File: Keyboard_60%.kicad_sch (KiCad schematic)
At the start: 50 parts, among them J3 Prog_conn, J5 Tag connect TC2030-CTX, SW2 Reset Switch, U3 nRF52840-QIAA-R/nRF52833-QIAA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, Y1 32MHz, Y2 32.768kHz

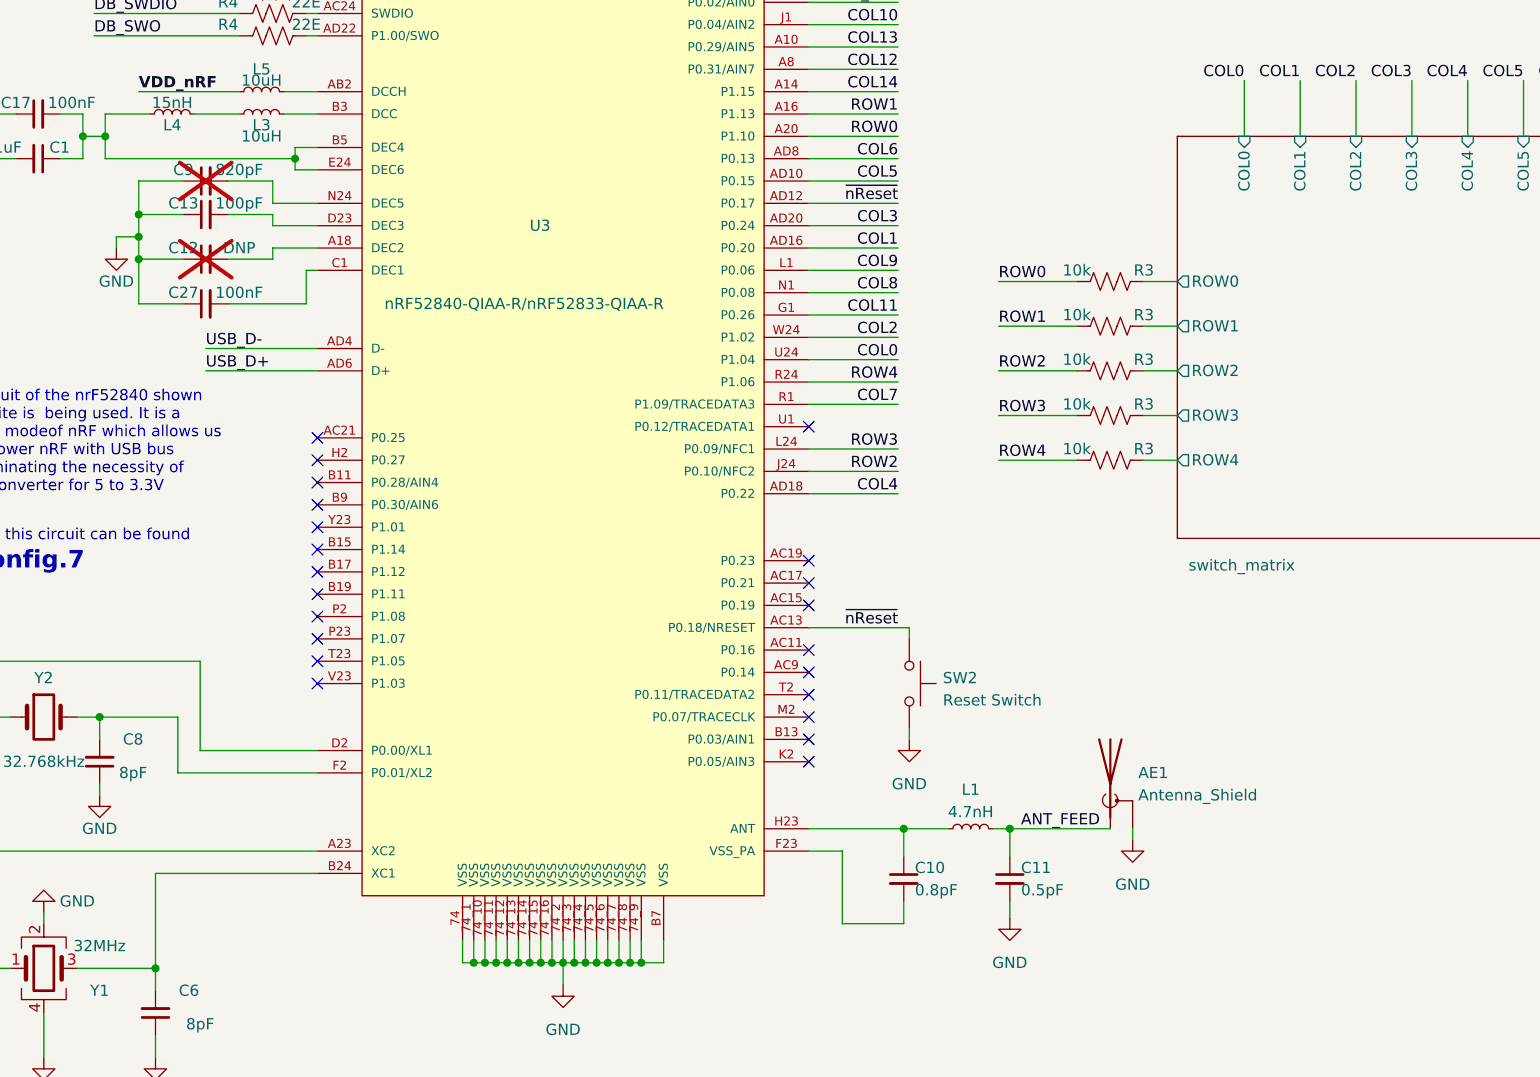
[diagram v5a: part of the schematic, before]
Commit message: Generated production files for PCB
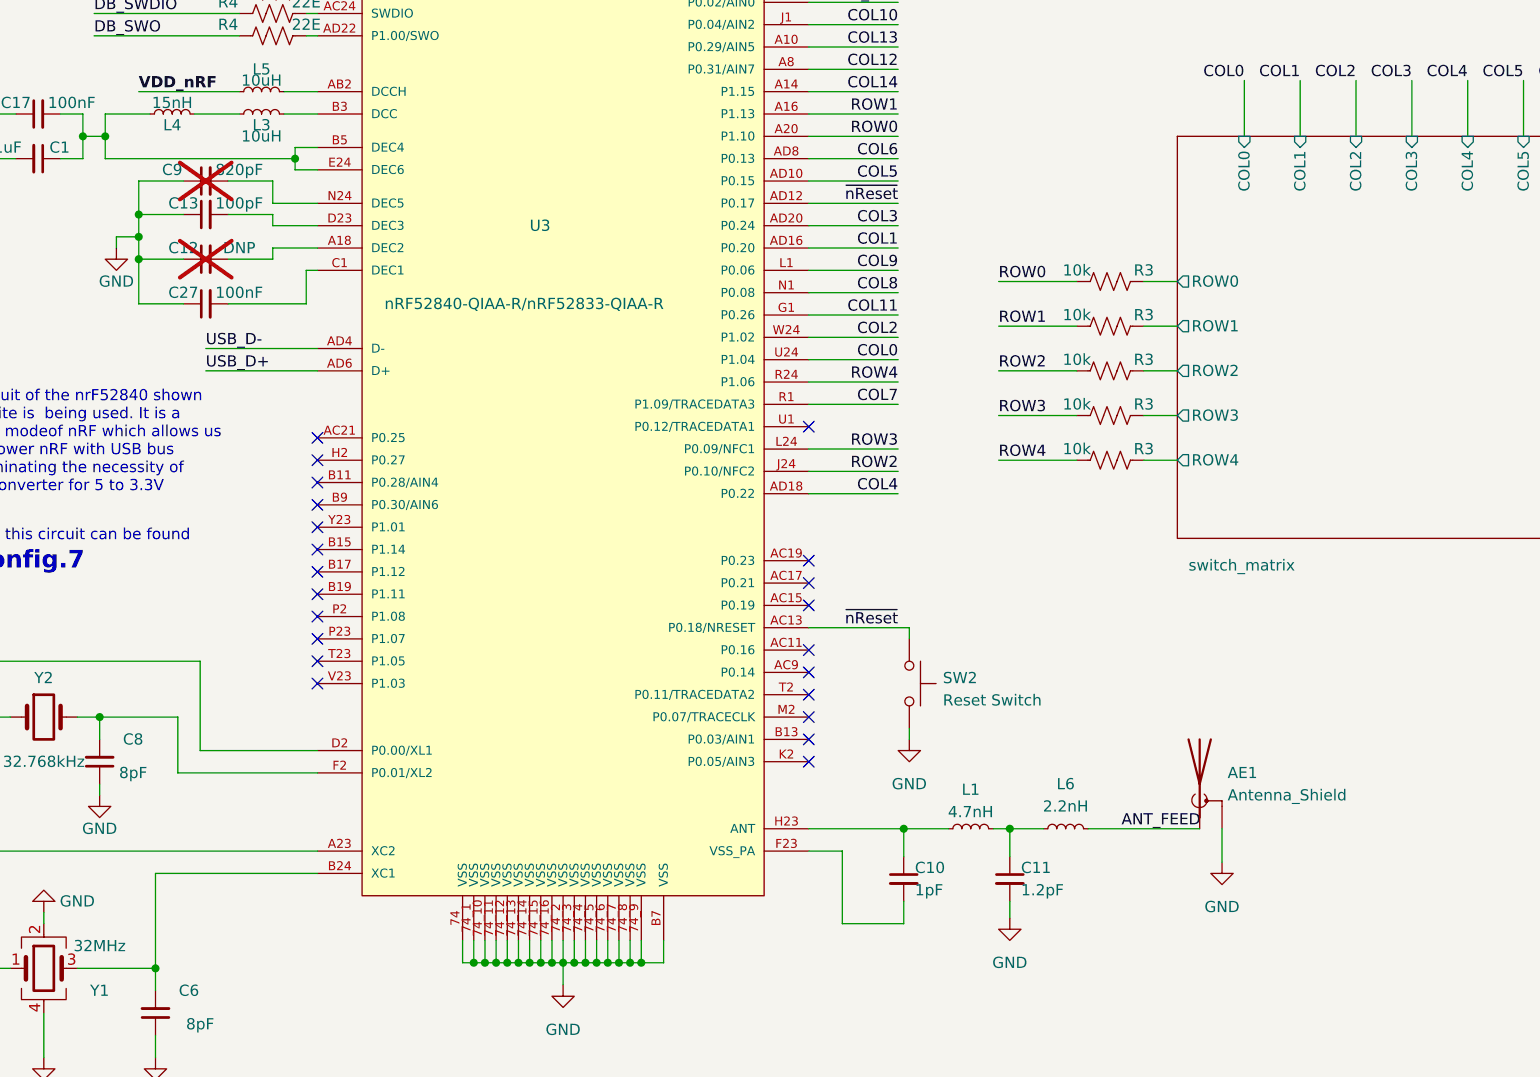
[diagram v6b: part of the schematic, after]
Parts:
- added L6: 2.2nH, keyboard:L_0402_1005Metric, symbol keyboard:L_Small
- C10: value 0.8pF -> 1pF; LCSC Part Number C325458 -> C309455; LCSC link https://www.lcsc.com/product-detail/Multilayer-Ceramic-Capacitors-MLCC-SMD-SMT_YAGEO-CC0402CRNPO9BNR80_C325458.html -> https://www.lcsc.com/product-detail/Multilayer-Ceramic-Capacitors-MLCC-SMD-SMT_YAGEO-CC0402BRNPO9BN1R0_C309455.html; PN CC0402CRNPO9BNR80 -> CC0402BRNPO9BN1R0
- C11: value 0.5pF -> 1.2pF; LCSC Part Number C327230 -> C327292; LCSC link https://www.lcsc.com/product-detail/Multilayer-Ceramic-Capacitors-MLCC-SMD-SMT_YAGEO-CC0402CRNPO9BNR50_C327230.html -> https://www.lcsc.com/product-detail/Multilayer-Ceramic-Capacitors-MLCC-SMD-SMT_YAGEO-CC0402BRNPO9BN1R2_C327292.html; PN CC0402CRNPO9BNR50 -> CC0402BRNPO9BN1R2
- L4: LCSC Part Number C97605 -> C86059; LCSC link https://www.lcsc.com/product-detail/Crystals_Seiko-SC-32S32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 -> https://www.lcsc.com/product-detail/Inductors-SMD_Murata-El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; PN SC-32S32.768kHz20PPM9pF -> LQG15HS15NJ02D
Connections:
- net ANT_FEED: now also L6.2; no longer C11.1, L1.2
- new net: C11.1, L1.2, L6.1
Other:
- moved on the sheet: AE1
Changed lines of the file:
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@@
     (stroke (width 0) (type default))
   )
-  (wire (pts (xy 142.24 166.37) (xy 153.67 166.37))
+  (wire (pts (xy 142.24 166.37) (xy 146.05 166.37))
     (stroke (width 0) (type default))
   )
@@
     (stroke (width 0) (type default))
   )
-  (wire (pts (xy 156.21 166.37) (xy 156.21 167.64))
+  (wire (pts (xy 166.37 166.37) (xy 166.37 170.18))
     (stroke (width 0) (type default))
   )
@@
     (stroke (width 0) (type default))
   )
+  (wire (pts (xy 151.13 166.37) (xy 163.83 166.37))
+    (stroke (width 0) (type default))
+  )
   (wire (pts (xy 58.42 101.6) (xy 58.42 100.33))
     (stroke (width 0) (type default))
@@
     (effects (font (size 1.27 1.27)) (justify right bottom))
   )
-  (label "ANT_FEED" (at 143.51 166.37 0) (fields_autoplaced)
+  (label "ANT_FEED" (at 154.94 166.37 0) (fields_autoplaced)
     (effects (font (size 1.27 1.27)) (justify left bottom))
   )
@@
   (symbol (lib_id "keyboard:C_Small") (at 50.8 92.71 90) (unit 1)
     (in_bom no) (on_board yes) (dnp yes)
-    (property "Reference" "C9" (at 48.26 91.44 90)
+    (property "Reference" "C9" (at 46.99 91.44 90)
       (effects (font (size 1.27 1.27)))
     )
@@
       (effects (font (size 1.27 1.27)) hide)
     )
-    (property "Datasheet" "https://datasheet.lcsc.com/lcsc/2304140030_Seiko-SC-32S32-768kHz20PPM9pF_C97605.pdf" (at 46.99 85.09 0)
+    (property "Datasheet" "https://datasheet.lcsc.com/lcsc/1811081610_Murata-Electronics-LQG15HS15NJ02D_C86059.pdf" (at 46.99 85.09 0)
       (effects (font (size 1.27 1.27)) hide)
     )
-    (property "LCSC Part Number" "C97605" (at 46.99 85.09 0)
+    (property "LCSC Part Number" "C86059" (at 46.99 85.09 0)
       (effects (font (size 1.27 1.27)) hide)
     )
-    (property "LCSC link" "https://www.lcsc.com/product-detail/Crystals_Seiko-SC-32S32-768kHz20PPM9pF_C97605.html" (at 46.99 85.09 0)
+    (property "LCSC link" "https://www.lcsc.com/product-detail/Inductors-SMD_Murata-Electronics-LQG15HS15NJ02D_C86059.html" (at 46.99 85.09 0)
       (effects (font (size 1.27 1.27)) hide)
     )
-    (property "PN" "SC-32S32.768kHz20PPM9pF" (at 46.99 85.09 0)
+    (property "PN" "LQG15HS15NJ02D" (at 46.99 85.09 0)
       (effects (font (size 1.27 1.27)) hide)
     )
@@
       (effects (font (size 1.27 1.27)) (justify left))
     )
-    (property "Value" "0.8pF" (at 131.445 173.355 0)
+    (property "Value" "1pF" (at 131.445 173.355 0)
       (effects (font (size 1.27 1.27)) (justify left))
     )
@@
       (effects (font (size 1.27 1.27)) hide)
     )
-    (property "Datasheet" "https://datasheet.lcsc.com/lcsc/1811070918_YAGEO-CC0402CRNPO9BNR80_C325458.pdf" (at 130.175 172.085 0)
+    (property "Datasheet" "https://datasheet.lcsc.com/lcsc/2304140030_YAGEO-CC0402BRNPO9BN1R0_C309455.pdf" (at 130.175 172.085 0)
       (effects (font (size 1.27 1.27)) hide)
     )
-    (property "PN" "CC0402CRNPO9BNR80" (at 130.175 172.085 0)
+    (property "PN" "CC0402BRNPO9BN1R0" (at 130.175 172.085 0)
       (effects (font (size 1.27 1.27)) hide)
     )
-    (property "LCSC Part Number" "C325458" (at 130.175 172.085 0)
+    (property "LCSC Part Number" "C309455" (at 130.175 172.085 0)
       (effects (font (size 1.27 1.27)) hide)
     )
-    (property "LCSC link" "https://www.lcsc.com/product-detail/Multilayer-Ceramic-Capacitors-MLCC-SMD-SMT_YAGEO-CC0402CRNPO9BNR80_C325458.html" (at 130.175 172.085 0)
+    (property "LCSC link" "https://www.lcsc.com/product-detail/Multilayer-Ceramic-Capacitors-MLCC-SMD-SMT_YAGEO-CC0402BRNPO9BN1R0_C309455.html" (at 130.175 172.085 0)
       (effects (font (size 1.27 1.27)) hide)
     )
@@
     )
   )
-  (symbol (lib_id "keyboard:Antenna_Shield") (at 153.67 161.29 0) (unit 1)
+  (symbol (lib_id "keyboard:Antenna_Shield") (at 163.83 161.29 0) (unit 1)
     (in_bom yes) (on_board yes) (dnp no) (fields_autoplaced)
-    (property "Reference" "AE1" (at 156.845 160.02 0)
+    (property "Reference" "AE1" (at 167.005 160.02 0)
       (effects (font (size 1.27 1.27)) (justify left))
     )
-    (property "Value" "Antenna_Shield" (at 156.845 162.56 0)
+    (property "Value" "Antenna_Shield" (at 167.005 162.56 0)
       (effects (font (size 1.27 1.27)) (justify left))
     )
-    (property "Footprint" "keyboard:BLE_ANTENNA" (at 153.67 158.75 0)
+    (property "Footprint" "keyboard:BLE_ANTENNA" (at 163.83 158.75 0)
       (effects (font (size 1.27 1.27)) hide)
     )
-    (property "Datasheet" "~" (at 153.67 158.75 0)
+    (property "Datasheet" "~" (at 163.83 158.75 0)
       (effects (font (size 1.27 1.27)) hide)
     )
-    (property "PN" "" (at 153.67 161.29 0)
+    (property "PN" "" (at 163.83 161.29 0)
       (effects (font (size 1.27 1.27)) hide)
     )
@@
     )
   )
-  (symbol (lib_id "power:GND") (at 156.21 167.64 0) (unit 1)
+  (symbol (lib_id "power:GND") (at 166.37 170.18 0) (unit 1)
     (in_bom yes) (on_board yes) (dnp no) (fields_autoplaced)
-    (property "Reference" "#PWR07" (at 156.21 173.99 0)
+    (property "Reference" "#PWR07" (at 166.37 176.53 0)
       (effects (font (size 1.27 1.27)) hide)
     )
-    (property "Value" "GND" (at 156.21 172.72 0)
+    (property "Value" "GND" (at 166.37 175.26 0)
       (effects (font (size 1.27 1.27)))
     )
-    (property "Footprint" "" (at 156.21 167.64 0)
+    (property "Footprint" "" (at 166.37 170.18 0)
       (effects (font (size 1.27 1.27)) hide)
     )
-    (property "Datasheet" "" (at 156.21 167.64 0)
+    (property "Datasheet" "" (at 166.37 170.18 0)
       (effects (font (size 1.27 1.27)) hide)
     )
@@
       (effects (font (size 1.27 1.27)) (justify left))
     )
-    (property "Value" "0.5pF" (at 143.51 173.355 0)
+    (property "Value" "1.2pF" (at 143.51 173.355 0)
       (effects (font (size 1.27 1.27)) (justify left))
     )
@@
       (effects (font (size 1.27 1.27)) hide)
     )
-    (property "Datasheet" "https://datasheet.lcsc.com/lcsc/1811141233_YAGEO-CC0402CRNPO9BNR50_C327230.pdf" (at 142.24 172.085 0)
+    (property "Datasheet" "https://datasheet.lcsc.com/lcsc/2304140030_YAGEO-CC0402BRNPO9BN1R2_C327292.pdf" (at 142.24 172.085 0)
       (effects (font (size 1.27 1.27)) hide)
     )
-    (property "PN" "CC0402CRNPO9BNR50" (at 142.24 172.085 0)
+    (property "PN" "CC0402BRNPO9BN1R2" (at 142.24 172.085 0)
       (effects (font (size 1.27 1.27)) hide)
     )
-    (property "LCSC Part Number" "C327230" (at 142.24 172.085 0)
+    (property "LCSC Part Number" "C327292" (at 142.24 172.085 0)
       (effects (font (size 1.27 1.27)) hide)
     )
-    (property "LCSC link" "https://www.lcsc.com/product-detail/Multilayer-Ceramic-Capacitors-MLCC-SMD-SMT_YAGEO-CC0402CRNPO9BNR50_C327230.html" (at 142.24 172.085 0)
+    (property "LCSC link" "https://www.lcsc.com/product-detail/Multilayer-Ceramic-Capacitors-MLCC-SMD-SMT_YAGEO-CC0402BRNPO9BN1R2_C327292.html" (at 142.24 172.085 0)
       (effects (font (size 1.27 1.27)) hide)
     )
@@
         )
       )
+    )
+  )
+  (symbol (lib_id "keyboard:L_Small") (at 148.59 166.37 90) (unit 1)
+    (in_bom yes) (on_board yes) (dnp no)
+    (property "Reference" "L6" (at 148.59 161.29 90)
+      (effects (font (size 1.27 1.27)))
+    )
+    (property "Value" "2.2nH" (at 148.59 163.83 90)
+      (effects (font (size 1.27 1.27)))
+    )
+    (property "Footprint" "keyboard:L_0402_1005Metric" (at 148.59 166.37 0)
+      (effects (font (size 1.27 1.27)) hide)
+    )
+    (property "Datasheet" "https://datasheet.lcsc.com/lcsc/2304140030_TDK-MLK1005S4N7ST000_C136252.pdf" (at 148.59 166.37 0)
+      (effects (font (size 1.27 1.27)) hide)
+    )
+    (property "PN" "MLK1005S4N7ST000" (at 148.59 166.37 0)
+      (effects (font (size 1.27 1.27)) hide)
+    )
+    (property "LCSC Part Number" "C136252" (at 148.59 166.37 0)
+      (effects (font (size 1.27 1.27)) hide)
+    )
+    (property "LCSC link" "https://www.lcsc.com/product-detail/Inductors-SMD_TDK-MLK1005S4N7ST000_C136252.html" (at 148.59 166.37 0)
+      (effects (font (size 1.27 1.27)) hide)
+    )
+    (pin "1")
+    (pin "2")
+    (instances
+      (project "Keyboard_60%"
+        (path "/ef112b03-6536-453f-8127-17d1495b48aa"
+          (reference "L6") (unit 1)
+        )
+      )
